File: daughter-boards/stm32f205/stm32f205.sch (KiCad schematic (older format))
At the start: 45 parts, among them P1 SAMTEC-QSE-020-01-F-D-A, P2 SAMTEC-QSE-020-01-F-D-A, U1 STM32F205RETx, Y1 Crystal_Small

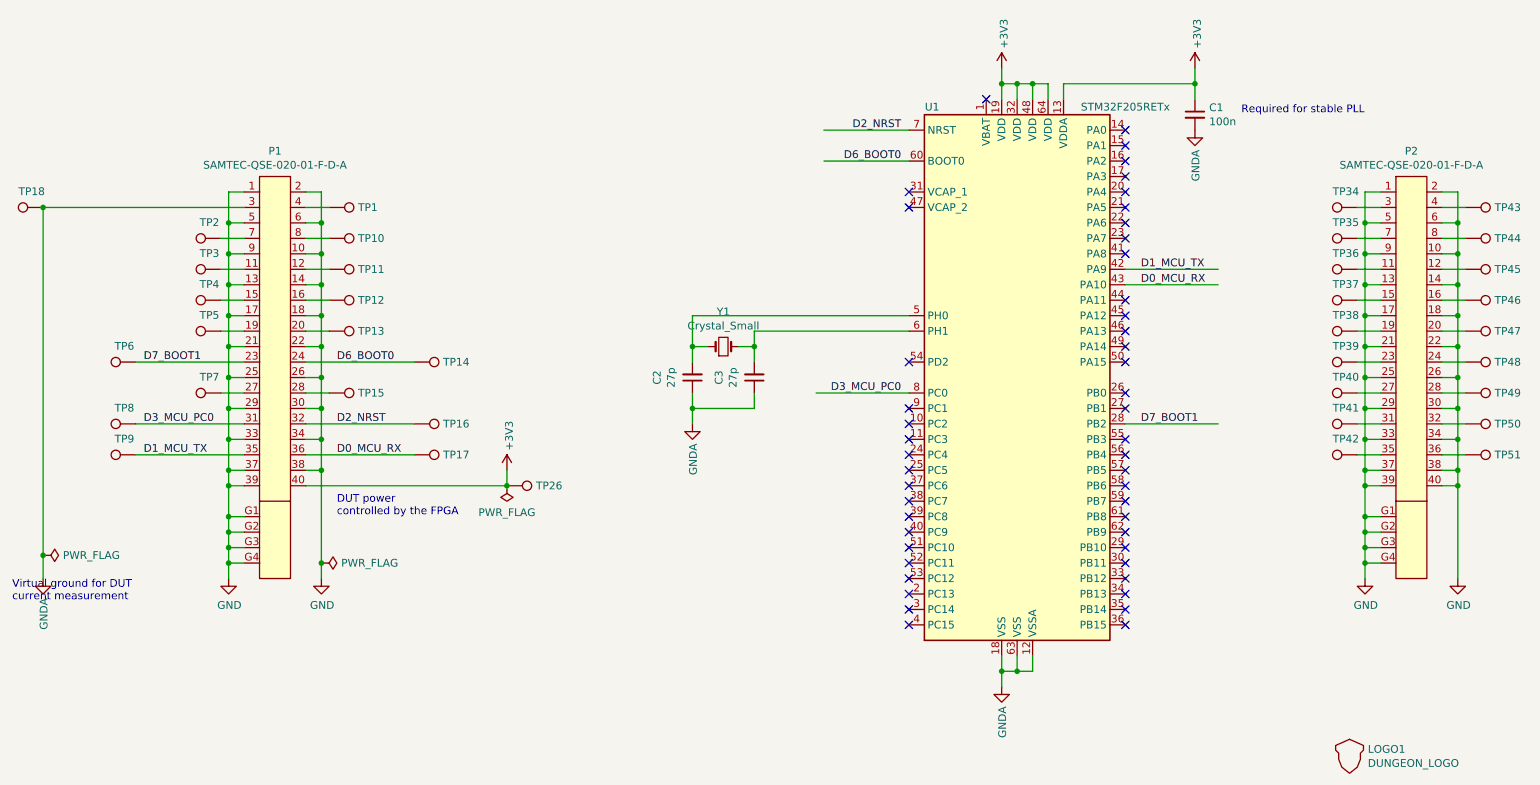
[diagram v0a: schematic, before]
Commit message: Updated daughterboards for the new Scaffold socket
Update breadboard, smartcard and STM32F205 daughterboards to fit the
new socket format of Scaffold v1.1 hardware.
Previous socket format is now deprecated.
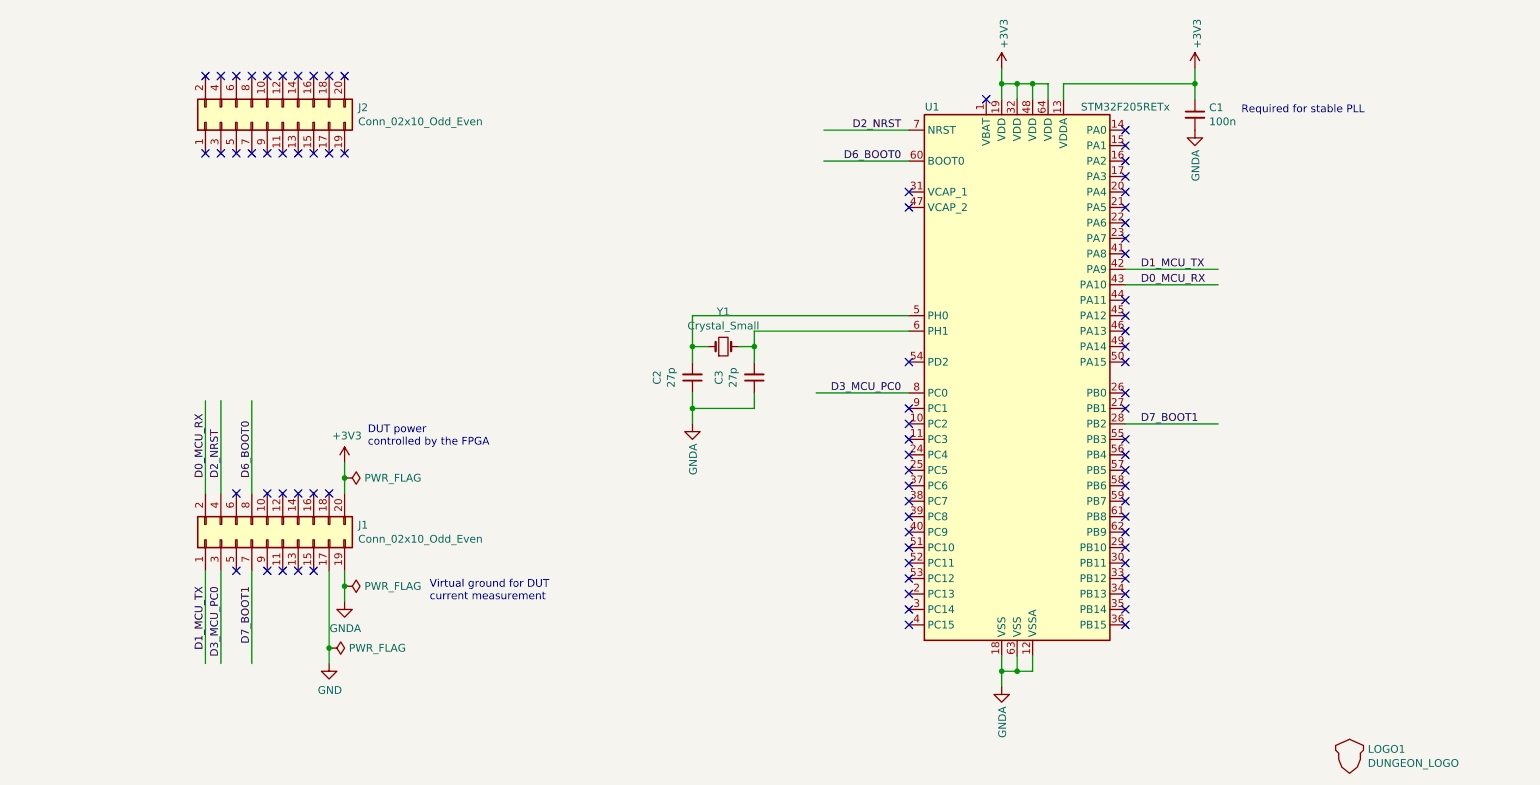
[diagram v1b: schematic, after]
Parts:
- removed P1, P2: SAMTEC-QSE-020-01-F-D-A, mykicadlibs:SAMTEC-QSE-020-01-F-D-A, symbol mylib:SAMTEC-QSE-020-01-F-D-A
- removed TP1, TP10, TP11, TP12, TP13, TP14, TP15, TP16, TP17, TP18, TP2, TP26, TP3, TP34, TP35, TP36, TP37, TP38, TP39, TP4, TP40, TP41, TP42, TP43, TP44, TP45, TP46, TP47, TP48, TP49, TP5, TP50, TP51, TP6, TP7, TP8, TP9: TestPoint, TestPoint:TestPoint_Pad_D1.5mm, symbol Connector:TestPoint
- added J1, J2: Conn_02x10_Odd_Even, Connector_PinSocket_2.54mm:PinSocket_2x10_P2.54mm_Vertical, symbol Connector_Generic:Conn_02x10_Odd_Even
- U1: footprint mykicadlibs:FLIP-ALLSOCKET-QFP64 -> mykicadlibs:ALLSOCKET-QFP64
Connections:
- wire segments 179 -> 48
- no-connect marks 48 -> 79

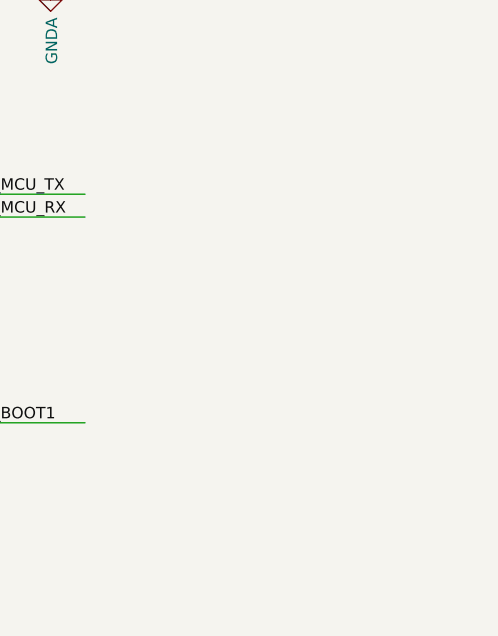
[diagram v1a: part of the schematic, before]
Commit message: Added breadboard space to STM32F205 daughterboard.
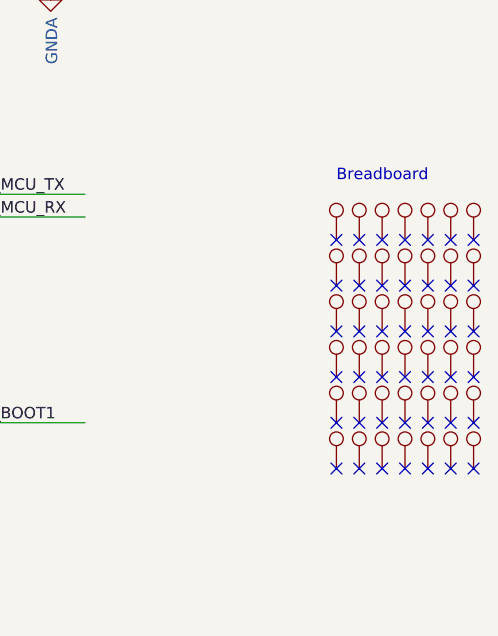
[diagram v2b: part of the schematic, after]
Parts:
- added TP1, TP10, TP11, TP12, TP13, TP14, TP15, TP16, TP17, TP18, TP19, TP2, TP20, TP21, TP22, TP23, TP24, TP25, TP26, TP27, TP28, TP29, TP3, TP30, TP31, TP32, TP33, TP34, TP35, TP36, TP37, TP38, TP39, TP4, TP40, TP41, TP42, TP5, TP6, TP7, TP8, TP9: TestPoint, mykicadlibs:TEST_BREADBOARD_RECTANGULAR, symbol Connector:TestPoint
- LOGO1: footprint mykicadlibs:donjon-3000 -> mykicadlibs:donjon-2000
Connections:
- no-connect marks 79 -> 121
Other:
- note added: "Breadboard"
